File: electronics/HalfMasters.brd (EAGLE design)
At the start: 87 x 80.8 mm, 17 parts, among them J1 F-1X04-SIP-100-40, U1 RASPBERRY_PICOSMD-TH, U2 L7805CV

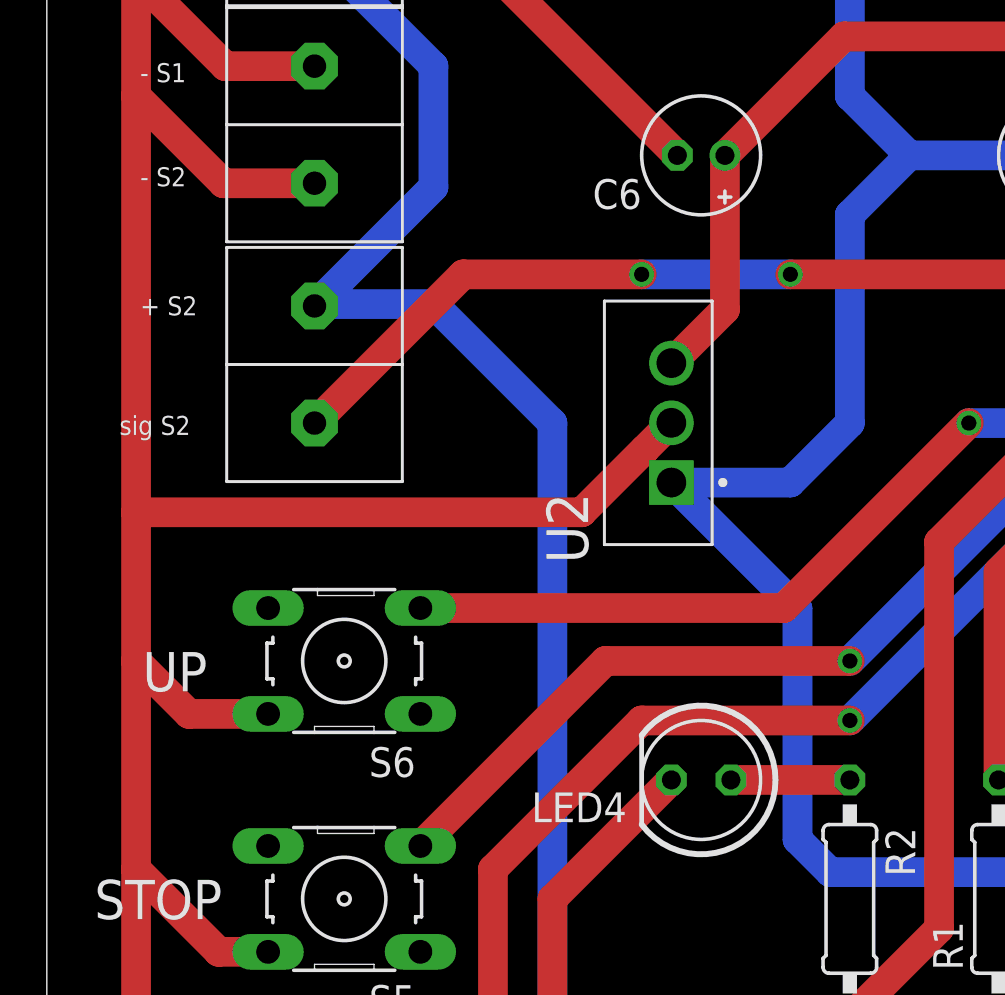
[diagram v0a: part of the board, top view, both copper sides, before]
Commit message: fix: 7805 position inverted vertically
No problem on the design, but this change will allow the voltage regulator to be placed bend in the PCB
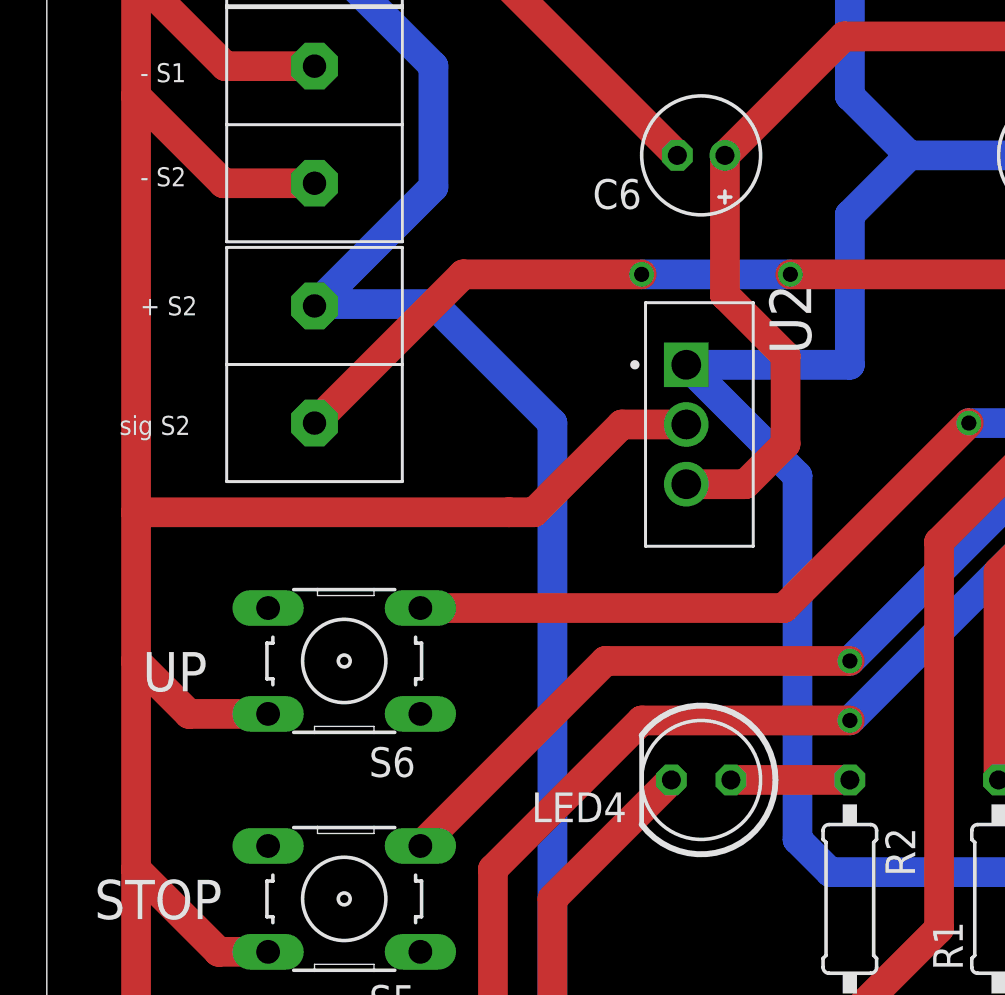
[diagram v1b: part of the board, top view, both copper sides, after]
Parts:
- moved U2 5.07 mm to (26.0, 54.6), turned to 270 degrees
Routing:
- net N$18: track 83.6 -> 92.2 mm
- net N$27: track 510.5 -> 511.1 mm
- net N$26: track 75.4 -> 76.0 mm
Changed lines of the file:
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@@
 <drawing>
 <settings>
-<setting alwaysvectorfont="yes"/>
+<setting alwaysvectorfont="no"/>
 <setting verticaltext="up"/>
 </settings>
@@
 <attribute name="VALUE" x="65.786" y="29.845" size="1.778" layer="27" rot="R90"/>
 </element>
-<element name="U2" library="L7805CV" package="TO255P1040X460X1968-3" value="L7805CV" x="25.4" y="49.53" smashed="yes" rot="R90">
-<attribute name="AVAILABILITY" value="In Stock" x="88.9" y="125.73" size="1.778" layer="27" rot="R90" display="off"/>
-<attribute name="DESCRIPTION" value=" Linear Voltage Regulator IC Positive Fixed 1 Output 1.5A TO-220 " x="88.9" y="125.73" size="1.778" layer="27" rot="R90" display="off"/>
-<attribute name="MF" value="STMicroelectronics" x="88.9" y="125.73" size="1.778" layer="27" rot="R90" display="off"/>
-<attribute name="MP" value="L7805CV" x="88.9" y="125.73" size="1.778" layer="27" rot="R90" display="off"/>
-<attribute name="NAME" x="21.845" y="46.08" size="1.778" layer="25" rot="R90"/>
-<attribute name="PACKAGE" value="TO-220-3 ON Semiconductor" x="88.9" y="125.73" size="1.778" layer="27" rot="R90" display="off"/>
-<attribute name="PRICE" value="None" x="88.9" y="125.73" size="1.778" layer="27" rot="R90" display="off"/>
-<attribute name="PURCHASE-URL" value="https://pricing.snapeda.com/search/part/L7805CV/?ref=eda" x="88.9" y="125.73" size="1.778" layer="27" rot="R90" display="off"/>
-<attribute name="VALUE" x="29.845" y="46.08" size="1.778" layer="27" rot="R90"/>
+<element name="U2" library="L7805CV" package="TO255P1040X460X1968-3" value="L7805CV" x="26.035" y="54.5592" smashed="yes" rot="R270">
+<attribute name="AVAILABILITY" value="In Stock" x="-37.465" y="-21.6408" size="1.778" layer="27" rot="R270" display="off"/>
+<attribute name="DESCRIPTION" value=" Linear Voltage Regulator IC Positive Fixed 1 Output 1.5A TO-220 " x="-37.465" y="-21.6408" size="1.778" layer="27" rot="R270" display="off"/>
+<attribute name="MF" value="STMicroelectronics" x="-37.465" y="-21.6408" size="1.778" layer="27" rot="R270" display="off"/>
+<attribute name="MP" value="L7805CV" x="-37.465" y="-21.6408" size="1.778" layer="27" rot="R270" display="off"/>
+<attribute name="NAME" x="29.59" y="58.0092" size="1.778" layer="25" rot="R270"/>
+<attribute name="PACKAGE" value="TO-220-3 ON Semiconductor" x="-37.465" y="-21.6408" size="1.778" layer="27" rot="R270" display="off"/>
+<attribute name="PRICE" value="None" x="-37.465" y="-21.6408" size="1.778" layer="27" rot="R270" display="off"/>
+<attribute name="PURCHASE-URL" value="https://pricing.snapeda.com/search/part/L7805CV/?ref=eda" x="-37.465" y="-21.6408" size="1.778" layer="27" rot="R270" display="off"/>
+<attribute name="VALUE" x="21.59" y="58.0092" size="1.778" layer="27" rot="R270"/>
 </element>
 <element name="LED3" library="led" library_urn="urn:adsk.eagle:library:259" package="LED5MM" package3d_urn="urn:adsk.eagle:package:15799/2" value="" x="26.67" y="24.13" smashed="yes" rot="R180">
@@
 <wire x1="44.45" y1="78.74" x2="44.45" y2="76.2" width="1.27" layer="1"/>
 <wire x1="74.93" y1="82.55" x2="48.26" y2="82.55" width="1.27" layer="1"/>
-<wire x1="27.686" y1="63.5" x2="27.686" y2="56.916" width="1.27" layer="1"/>
-<wire x1="27.686" y1="56.916" x2="25.4" y2="54.63" width="1.27" layer="1"/>
 <wire x1="27.686" y1="63.5" x2="32.766" y2="68.58" width="1.27" layer="1"/>
 <wire x1="32.766" y1="68.58" x2="40.64" y2="68.58" width="1.27" layer="1"/>
 <wire x1="40.64" y1="68.58" x2="44.45" y2="72.39" width="1.27" layer="1"/>
 <wire x1="44.45" y1="72.39" x2="44.45" y2="76.2" width="1.27" layer="1"/>
+<wire x1="27.686" y1="63.5" x2="27.686" y2="57.531" width="1.27" layer="1"/>
+<wire x1="27.686" y1="57.531" x2="30.2768" y2="54.9402" width="1.27" layer="1"/>
+<wire x1="30.2768" y1="54.9402" x2="30.2768" y2="51.181" width="1.27" layer="1"/>
+<wire x1="28.555" y1="49.4592" x2="26.035" y2="49.4592" width="1.27" layer="1"/>
+<wire x1="30.2768" y1="51.181" x2="28.555" y2="49.4592" width="1.27" layer="1"/>
 <wire x1="74.77" y1="72.39" x2="73.66" y2="72.39" width="0" layer="19" extent="1-1"/>
 </signal>
@@
 <wire x1="35.56" y1="63.5" x2="33.02" y2="66.04" width="1.27" layer="16"/>
 <wire x1="35.56" y1="63.5" x2="33.02" y2="60.96" width="1.27" layer="16"/>
-<wire x1="33.02" y1="60.96" x2="33.02" y2="52.07" width="1.27" layer="16"/>
-<wire x1="33.02" y1="52.07" x2="30.48" y2="49.53" width="1.27" layer="16"/>
-<wire x1="30.48" y1="49.53" x2="25.4" y2="49.53" width="1.27" layer="16"/>
+<wire x1="33.02" y1="60.96" x2="33.02" y2="54.5592" width="1.27" layer="16"/>
+<wire x1="33.02" y1="54.5592" x2="26.035" y2="54.5592" width="1.27" layer="16"/>
 <contactref element="J1" pad="2"/>
 <wire x1="46.2534" y1="32.893" x2="32.1818" y2="32.893" width="1.27" layer="16"/>
-<wire x1="30.7848" y1="44.1452" x2="25.4" y2="49.53" width="1.27" layer="16"/>
+<wire x1="30.7848" y1="49.8094" x2="26.035" y2="54.5592" width="1.27" layer="16"/>
 <wire x1="32.1818" y1="32.893" x2="30.7848" y2="34.29" width="1.27" layer="16"/>
-<wire x1="30.7848" y1="34.29" x2="30.7848" y2="44.1452" width="1.27" layer="16"/>
+<wire x1="30.7848" y1="34.29" x2="30.7848" y2="49.8094" width="1.27" layer="16"/>
 </signal>
 <signal name="N$27">
@@
 <wire x1="74.77" y1="31.75" x2="81.28" y2="31.75" width="1.27" layer="1"/>
 <wire x1="81.28" y1="31.75" x2="82.55" y2="33.02" width="1.27" layer="1"/>
-<wire x1="25.4" y1="52.08" x2="24.2622" y2="50.9422" width="1.27" layer="1"/>
-<wire x1="24.2622" y1="50.9422" x2="24.25561875" y2="50.9422" width="0.6096" layer="1"/>
-<wire x1="21.57341875" y1="48.26" x2="2.54" y2="48.26" width="1.27" layer="1"/>
-<wire x1="24.25561875" y1="50.9422" x2="21.57341875" y2="48.26" width="1.27" layer="1"/>
+<wire x1="18.4658" y1="48.26" x2="2.54" y2="48.26" width="1.27" layer="1"/>
 <wire x1="8.1788" y1="19.3294" x2="2.54" y2="24.9682" width="1.27" layer="1"/>
 <wire x1="8.1788" y1="29.4894" x2="6.0706" y2="29.4894" width="1.27" layer="1"/>
@@
 <wire x1="48.3108" y1="31.75" x2="54.77" y2="31.75" width="1.27" layer="1"/>
 <wire x1="46.9138" y1="30.353" x2="48.3108" y2="31.75" width="1.27" layer="1"/>
+<wire x1="26.035" y1="52.0092" x2="23.2818" y2="52.0092" width="1.27" layer="1"/>
+<wire x1="19.5326" y1="48.26" x2="18.4658" y2="48.26" width="1.27" layer="1"/>
+<wire x1="23.2818" y1="52.0092" x2="19.5326" y2="48.26" width="1.27" layer="1"/>
 <wire x1="73.66" y1="69.85" x2="74.77" y2="69.85" width="0" layer="19" extent="1-1"/>
 <wire x1="73.66" y1="57.15" x2="73.66" y2="69.85" width="0" layer="19" extent="1-1"/>

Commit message: refacotr: code upload to github
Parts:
- added S1: (no value), switch:255SB
- moved J1 40.2 mm to (83.6, 48.8)
- moved S6 40.2 mm to (48.8, 56.6)
- moved U2 40.2 mm to (63.4, 69.2)
- moved C5 40.2 mm to (79.3, 78.2)
- moved LED3 40.2 mm to (64.1, 38.8)
- moved LED4 40.2 mm to (64.1, 51.5)
- moved S5 40.2 mm to (48.8, 46.4)
- moved S7 40.2 mm to (48.8, 36.2)
- moved U$1 40.2 mm to (47.5, 69.3)
- moved U$2 40.2 mm to (47.5, 79.4)
- moved U$3 40.2 mm to (47.5, 89.6)
- moved U$4 40.2 mm to (64.1, 90.9)
- moved U$5 40.2 mm to (79.3, 90.9)
- moved U1 40.2 mm to (102.2, 65.5)
- moved R1 40.2 mm to (76.8, 46.4)
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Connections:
- new net N$3: S1.3, U$5.P0
- new net N$7: S1.2, U1.39, U1.P$39
- net N$18: now also S1.1; no longer U$5.P0, U1.39, U1.P$39
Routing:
- net N$7: track 0.00 -> 78.9 mm
- net N$18: track 92.2 -> 30.9 mm
- net N$3: track 0.00 -> 20.9 mm
- net N$27: track 511.1 -> 493.7 mm
